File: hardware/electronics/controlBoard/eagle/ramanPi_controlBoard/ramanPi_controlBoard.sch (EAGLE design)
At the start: 19 parts

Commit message: update
updated all boards and schematics
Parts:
- added FID1, FID2: FIDUCIAL1X2, SparkFun-Aesthetics:FIDUCIAL1X2
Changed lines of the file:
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@@
 <part name="JP1" library="SparkFun-Connectors" deviceset="M07" device=""/>
 <part name="JP2" library="SparkFun-Connectors" deviceset="M07" device=""/>
+<part name="FID1" library="SparkFun-Aesthetics" deviceset="FIDUCIAL" device="1X2"/>
+<part name="FID2" library="SparkFun-Aesthetics" deviceset="FIDUCIAL" device="1X2"/>
 </parts>
 <sheets>
@@
 <instance part="JP1" gate="G$1" x="121.92" y="17.78" rot="R90"/>
 <instance part="JP2" gate="G$1" x="116.84" y="182.88" rot="R270"/>
+<instance part="FID1" gate="G$1" x="220.98" y="180.34"/>
+<instance part="FID2" gate="G$1" x="228.6" y="180.34"/>
 </instances>
 <busses>

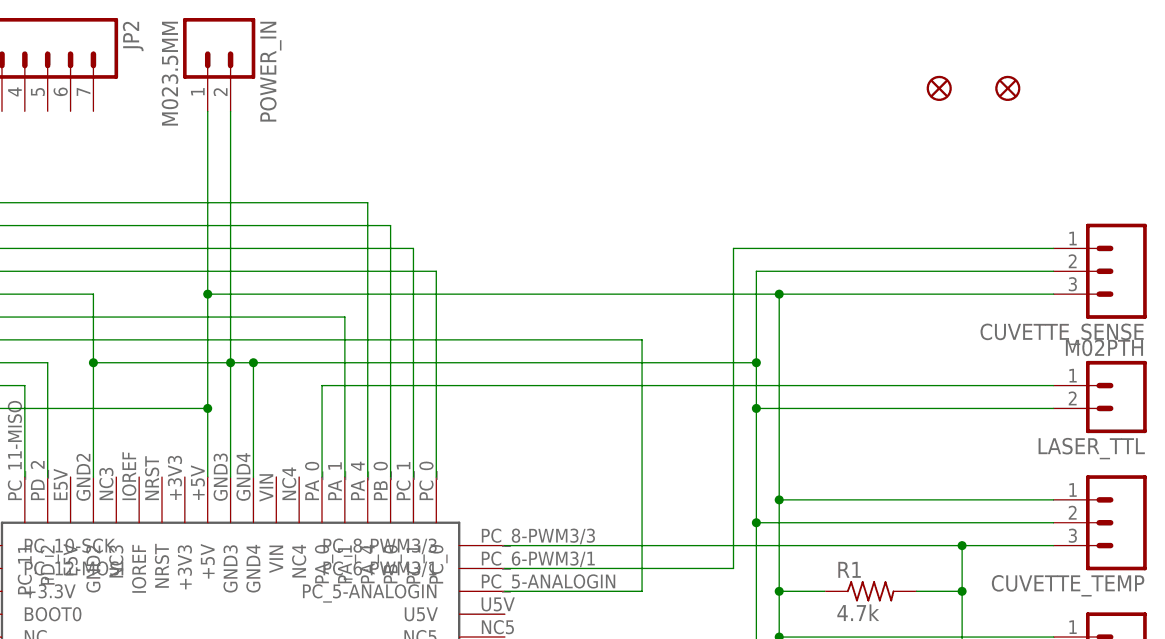
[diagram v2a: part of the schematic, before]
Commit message: added reset circuitry to all stm32 boards
added reset circuitry for raspi to reset each board from remote.
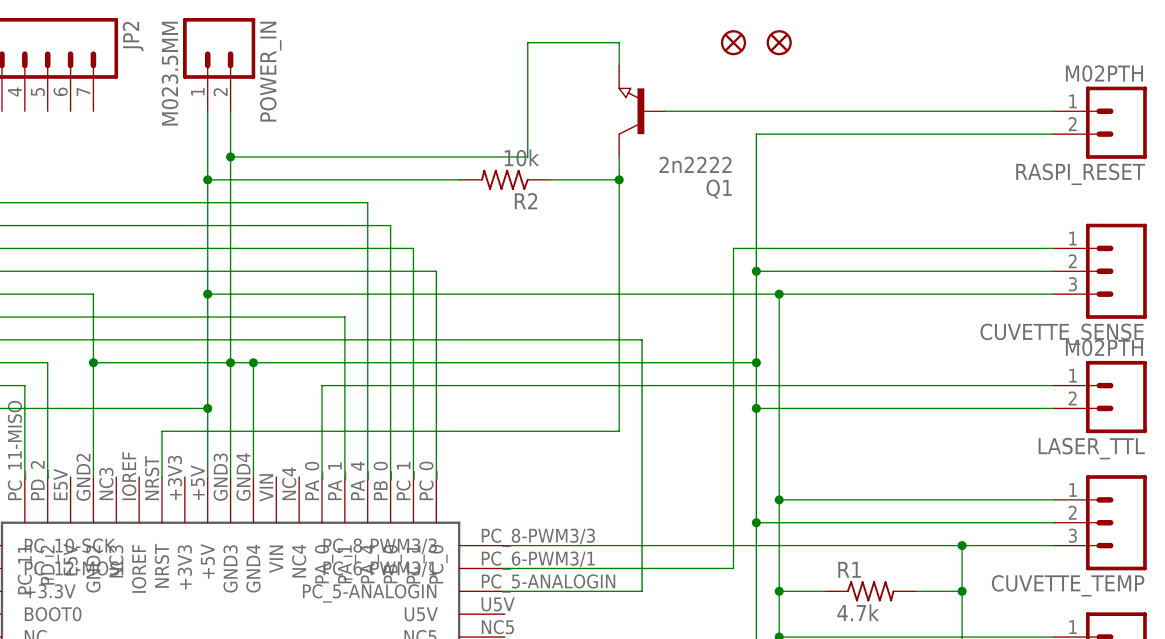
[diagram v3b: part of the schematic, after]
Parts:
- added Q1: 2n2222, semicon-smd-ipc:NPN-TRANSISTOR_SOT23
- added R2: 10k, adafruit:R-US_M1206
- added RASPI_RESET: M02PTH, SparkFun-Connectors:M02PTH
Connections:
- new net N$49: Q1.C, R2.1, U$1.NRST
- new net N$50: Q1.B, RASPI_RESET.1
- net +5V: now also R2.2
- net GROUND: now also Q1.E, RASPI_RESET.2
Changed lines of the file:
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@@
 <part name="FID1" library="SparkFun-Aesthetics" deviceset="FIDUCIAL" device="1X2"/>
 <part name="FID2" library="SparkFun-Aesthetics" deviceset="FIDUCIAL" device="1X2"/>
+<part name="Q1" library="semicon-smd-ipc" deviceset="NPN-TRANSISTOR_" device="SOT23" value="2n2222"/>
+<part name="R2" library="adafruit" deviceset="R-US_" device="M1206" value="10k"/>
+<part name="RASPI_RESET" library="SparkFun-Connectors" deviceset="M02" device="PTH"/>
 </parts>
 <sheets>
@@
 <instance part="JP1" gate="G$1" x="121.92" y="17.78" rot="R90"/>
 <instance part="JP2" gate="G$1" x="116.84" y="182.88" rot="R270"/>
-<instance part="FID1" gate="G$1" x="220.98" y="180.34"/>
-<instance part="FID2" gate="G$1" x="228.6" y="180.34"/>
+<instance part="FID1" gate="G$1" x="198.12" y="185.42"/>
+<instance part="FID2" gate="G$1" x="203.2" y="185.42"/>
+<instance part="Q1" gate="G$1" x="187.96" y="177.8" rot="R180"/>
+<instance part="R2" gate="G$1" x="172.72" y="170.18" rot="R180"/>
+<instance part="RASPI_RESET" gate="G$1" x="241.3" y="177.8" rot="R180"/>
 </instances>
 <busses>
@@
 <pinref part="POWER_CONTROL_BOARD" gate="G$1" pin="1"/>
 <pinref part="POWER_IN" gate="G$1" pin="1"/>
-<wire x1="139.7" y1="157.48" x2="139.7" y2="177.8" width="0.1524" layer="91"/>
+<wire x1="139.7" y1="157.48" x2="139.7" y2="170.18" width="0.1524" layer="91"/>
 <junction x="139.7" y="157.48"/>
+<pinref part="R2" gate="G$1" pin="2"/>
+<wire x1="139.7" y1="170.18" x2="139.7" y2="177.8" width="0.1524" layer="91"/>
+<wire x1="139.7" y1="170.18" x2="167.64" y2="170.18" width="0.1524" layer="91"/>
+<junction x="139.7" y="170.18"/>
 </segment>
 </net>
@@
 <wire x1="35.56" y1="106.68" x2="73.66" y2="106.68" width="0.1524" layer="91"/>
 <pinref part="POWER_IN" gate="G$1" pin="2"/>
-<wire x1="142.24" y1="149.86" x2="142.24" y2="177.8" width="0.1524" layer="91"/>
-</segment>
-</net>
+<wire x1="142.24" y1="149.86" x2="142.24" y2="172.72" width="0.1524" layer="91"/>
+<pinref part="Q1" gate="G$1" pin="E"/>
+<wire x1="142.24" y1="172.72" x2="142.24" y2="177.8" width="0.1524" layer="91"/>
+<wire x1="185.42" y1="182.88" x2="185.42" y2="185.42" width="0.1524" layer="91"/>
+<wire x1="185.42" y1="185.42" x2="175.26" y2="185.42" width="0.1524" layer="91"/>
+<wire x1="175.26" y1="185.42" x2="175.26" y2="172.72" width="0.1524" layer="91"/>
+<wire x1="175.26" y1="172.72" x2="142.24" y2="172.72" width="0.1524" layer="91"/>
+<junction x="142.24" y="172.72"/>
+<pinref part="RASPI_RESET" gate="G$1" pin="2"/>
+<wire x1="233.68" y1="175.26" x2="200.66" y2="175.26" width="0.1524" layer="91"/>
+<wire x1="200.66" y1="175.26" x2="200.66" y2="160.02" width="0.1524" layer="91"/>
+<junction x="200.66" y="160.02"/>
+</segment>
+</net>
+<net name="N$49" class="0">
+<segment>
+<pinref part="U$1" gate="G$1" pin="NRST"/>
+<wire x1="134.62" y1="137.16" x2="134.62" y2="142.24" width="0.1524" layer="91"/>
+<wire x1="134.62" y1="142.24" x2="185.42" y2="142.24" width="0.1524" layer="91"/>
+<pinref part="Q1" gate="G$1" pin="C"/>
+<wire x1="185.42" y1="142.24" x2="185.42" y2="170.18" width="0.1524" layer="91"/>
+<pinref part="R2" gate="G$1" pin="1"/>
+<wire x1="185.42" y1="170.18" x2="185.42" y2="172.72" width="0.1524" layer="91"/>
+<wire x1="177.8" y1="170.18" x2="185.42" y2="170.18" width="0.1524" layer="91"/>
+<junction x="185.42" y="170.18"/>
+</segment>
+</net>
+<net name="N$50" class="0">
+<segment>
+<pinref part="Q1" gate="G$1" pin="B"/>
+<pinref part="RASPI_RESET" gate="G$1" pin="1"/>
+<wire x1="190.5" y1="177.8" x2="233.68" y2="177.8" width="0.1524" layer="91"/>
+</segment>
+</net>
